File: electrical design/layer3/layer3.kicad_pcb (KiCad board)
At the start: 2 copper layers, 150 x 137.9 mm, 33 parts, among them J1 SH1.0 5P, J10 SH1.0 2P, J11 LAYER1, J2 SH1.0 5P, J3 SH1.0 5P, J4 SH1.0 5P, J5 XH2.54 5P, J6 CAMERA1, J7 CAMERA2, J8 COMPASS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

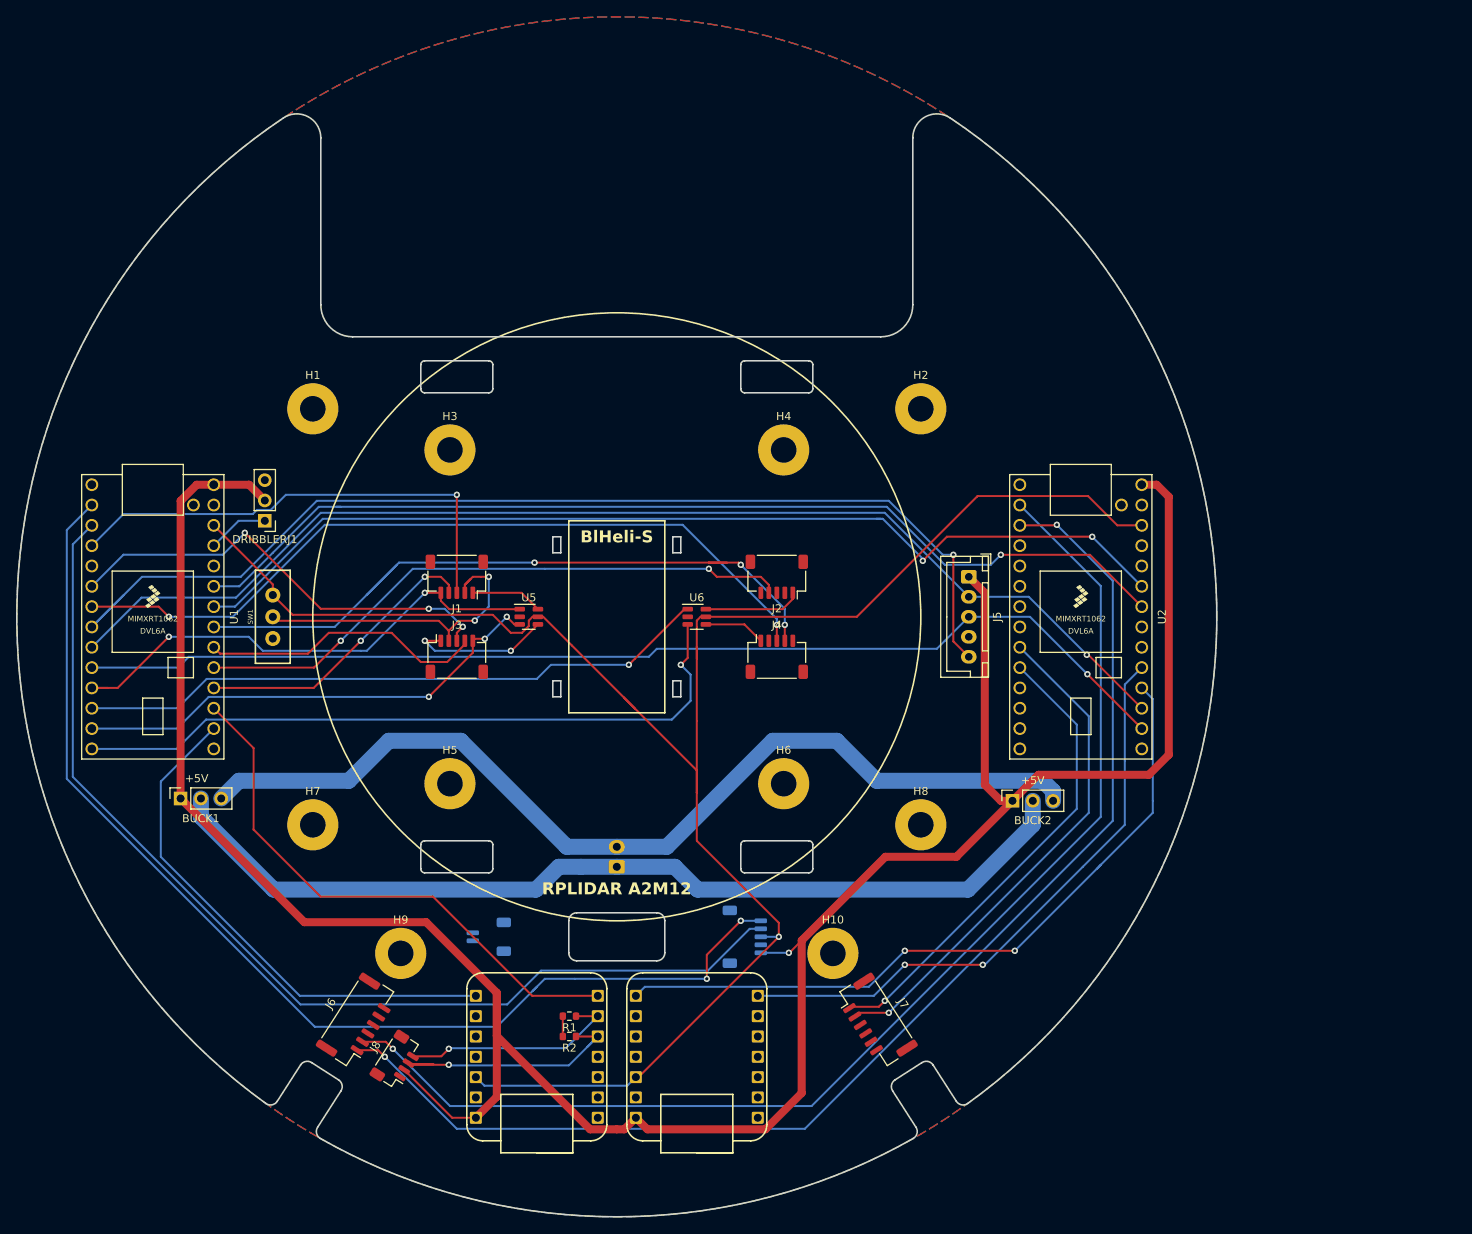
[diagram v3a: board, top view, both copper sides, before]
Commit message: update pcbs for dual camera design
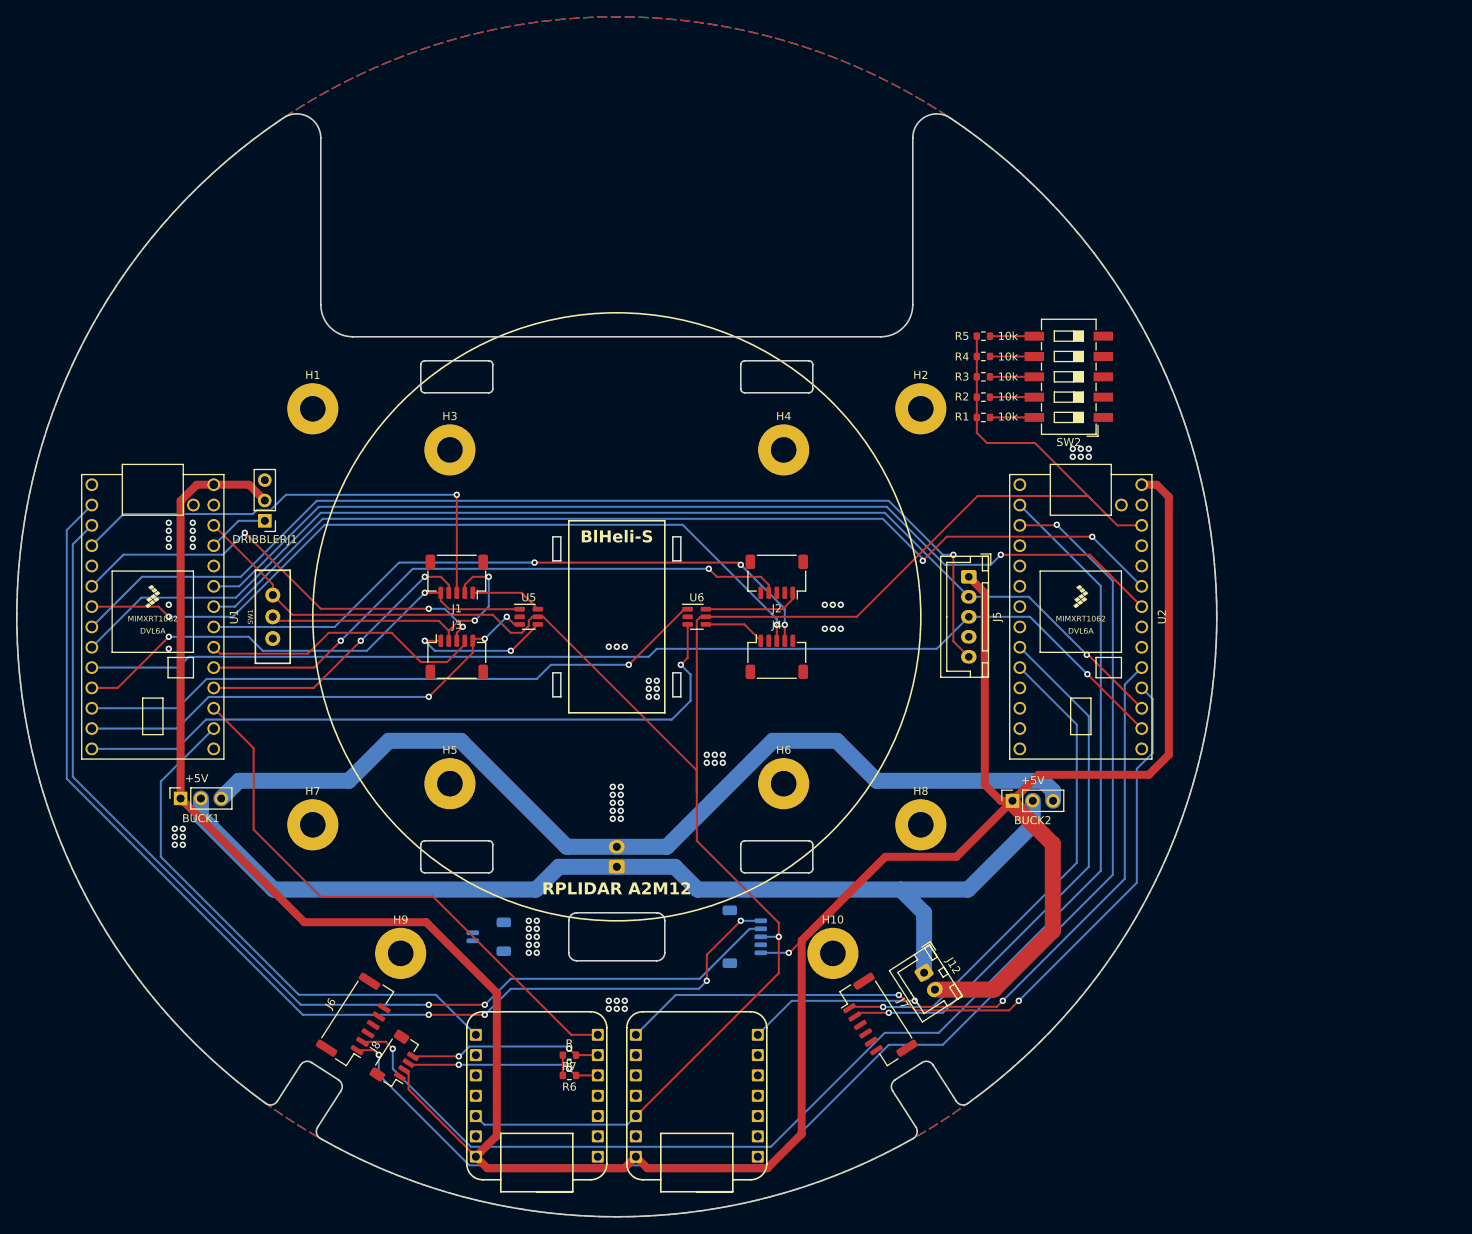
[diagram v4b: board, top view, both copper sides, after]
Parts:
- added J12: XH2.54 2P, Connector_JST:JST_XH_B2B-XH-A_1x02_P2.50mm_Vertical, F.Cu at (143.4, 149.5)
- added R1: 10k, Resistor_SMD:R_0603_1608Metric, F.Cu at (150.8, 80.1)
- added R2: 10k, Resistor_SMD:R_0603_1608Metric, F.Cu at (150.8, 77.5)
- added R3: 10k, Resistor_SMD:R_0603_1608Metric, F.Cu at (150.8, 75.0)
- added R4: 10k, Resistor_SMD:R_0603_1608Metric, F.Cu at (150.8, 72.5)
- added R5: 10k, Resistor_SMD:R_0603_1608Metric, F.Cu at (150.8, 69.9)
- added SW2: SW_DIP_x05, Button_Switch_SMD:SW_DIP_SPSTx05_Slide_6.7x14.26mm_W8.61mm_P2.54mm_LowProfile, F.Cu at (161.5, 75.0)
- J9: value Conn_01x02_Pin -> XH2.54 2P
- moved R6 4.87 mm to (99.1, 162.3)
- moved R7 4.87 mm to (99.1, 159.8)
- moved U3 4.87 mm to (95.0, 164.9)
- moved U4 4.87 mm to (115.0, 164.9)
- renumbered R2 to R6, R1 to R7
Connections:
- U2 pad 2: unconnected-(U2-Pad2) -> /STRAT1
- U2 pad 3: unconnected-(U2-Pad3) -> /STRAT2
- U2 pad 4: unconnected-(U2-Pad4) -> /STRAT3
- U2 pad 5: unconnected-(U2-Pad5) -> /STRAT4
- U2 pad 6: unconnected-(U2-Pad6) -> /STRAT5
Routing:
- net +5V: track 326.2 -> 368.3 mm
- net +3V3: track 237.8 -> 268.8 mm
- net GNDPWR: track 118.8 -> 130.4 mm
- net /CAM1TX: track 153.9 -> 163.4 mm
- net /CAM1RX: track 159.0 -> 168.2 mm
- net /IMUSDA: track 33.0 -> 24.5 mm, vias 1 -> 2
- net /M4CS: track 88.7 -> 81.1 mm
- net /BTTX: track 91.0 -> 98.0 mm
- net /BTRX: track 75.3 -> 81.9 mm
- net /LIDARPWM: track 136.2 -> 130.6 mm
- net /STRAT5: track 0.00 -> 5.54 mm
- net /STRAT4: track 0.00 -> 5.54 mm
- net /STRAT3: track 0.00 -> 5.54 mm
- net /STRAT2: track 0.00 -> 5.54 mm
- net /STRAT1: track 0.00 -> 5.54 mm
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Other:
- outline, holes or cut-outs redrawn

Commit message: change EN switch to larger one
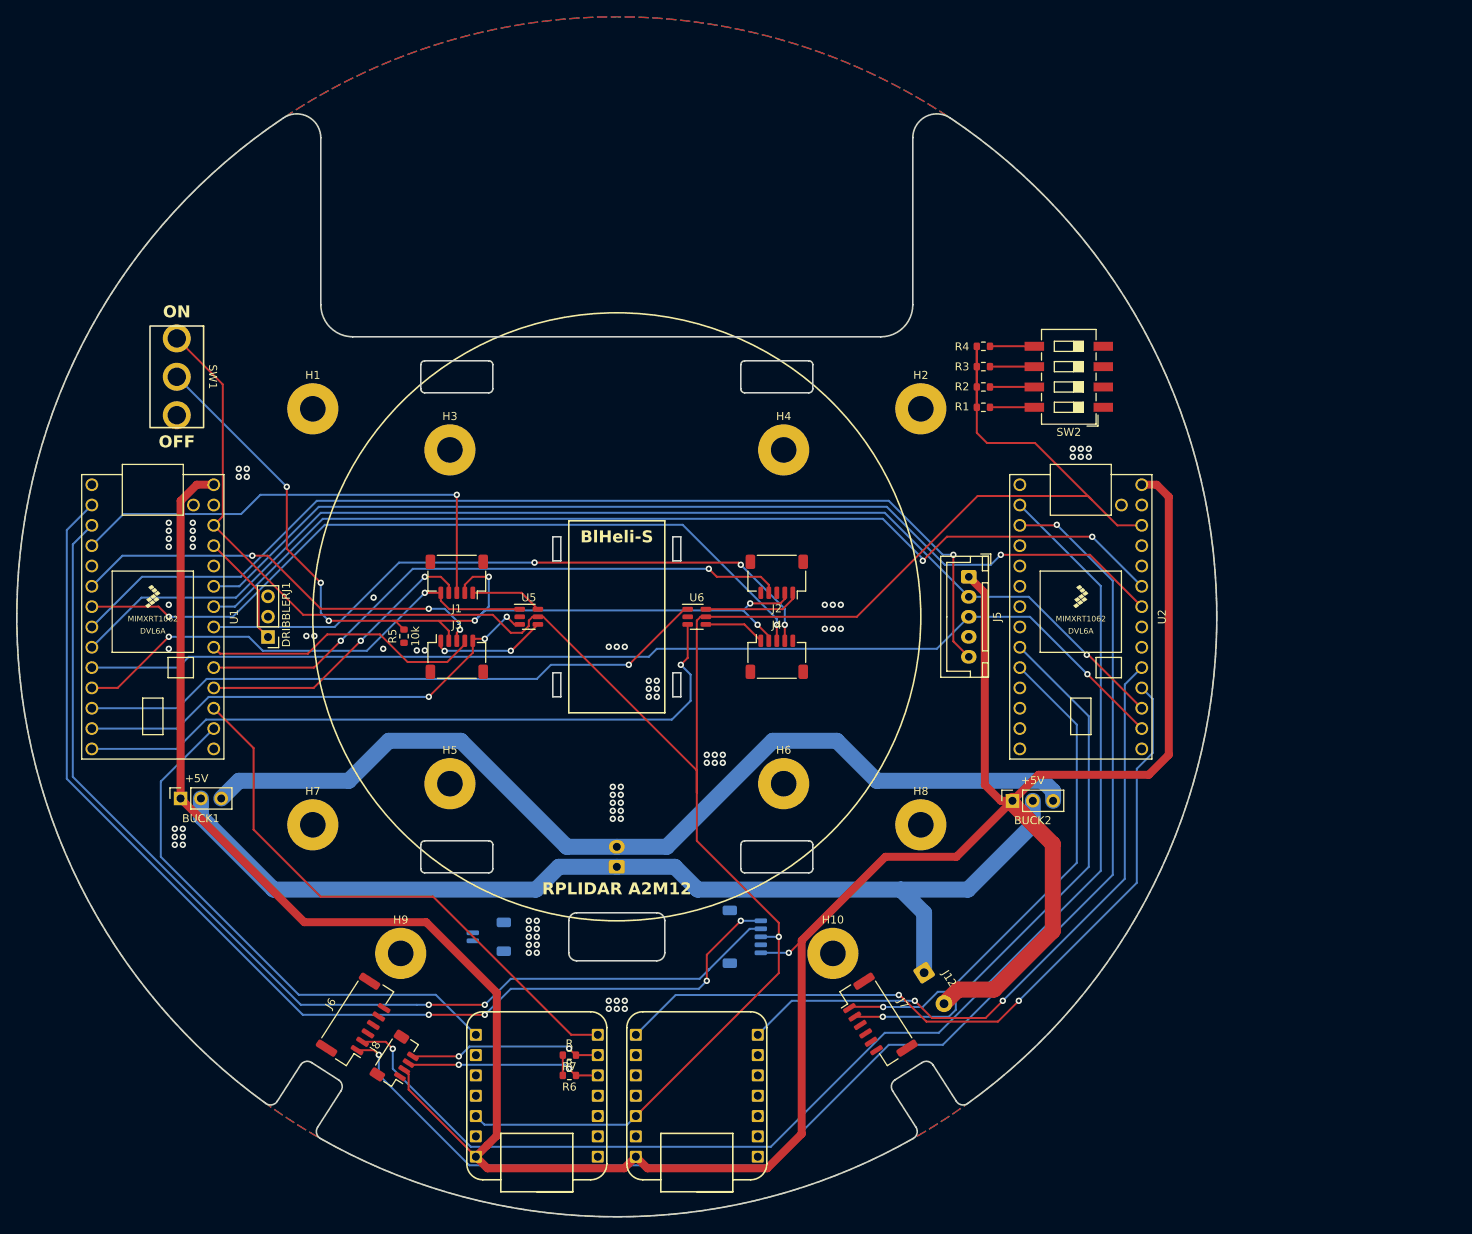
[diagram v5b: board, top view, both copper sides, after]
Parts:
- J12: footprint Connector_JST:JST_XH_B2B-XH-A_1x02_P2.50mm_Vertical -> Connector_Wire:SolderWire-0.5sqmm_1x02_P4.6mm_D0.9mm_OD2.1mm
- SW1: value SW_DPDT_x2 -> SW_SPDT; footprint Switches:SWITCH_SPDT_PTH_11.6X4.0MM_LOCK -> Switches:SWITCH_SPDT_PTH_12.7X6.7MM
- SW2: value SW_DIP_x05 -> SW_DIP_x04; footprint Button_Switch_SMD:SW_DIP_SPSTx05_Slide_6.7x14.26mm_W8.61mm_P2.54mm_LowProfile -> Button_Switch_SMD:SW_DIP_SPSTx04_Slide_6.7x11.72mm_W8.61mm_P2.54mm_LowProfile
- moved R5 81.6 mm to (78.4, 107.4), turned to 90 degrees
- moved SW1 32.3 mm to (50.0, 75.0), turned to -90 degrees
- moved DRIBBLERJ1 14.5 mm to (61.4, 107.5)
- moved R2 1.27 mm to (150.8, 76.3)
- moved R1 1.27 mm to (150.8, 78.8)
- moved R3 1.27 mm to (150.8, 73.7)
- moved R4 1.27 mm to (150.8, 71.2)
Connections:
- DRIBBLERJ1 pad 2: +5V -> unconnected-(DRIBBLERJ1-Pin_2-Pad2)
- R5 pad 1: +3V3 -> GNDD
- R5 pad 2: /STRAT5 -> /EN
- SW2 pad 5: GNDD -> /STRAT4
- SW2 pad 6: /STRAT5 -> /STRAT3
- SW2 pad 7: /STRAT4 -> /STRAT2
- SW2 pad 8: /STRAT3 -> /STRAT1
- U2 pad 6: /STRAT5 -> unconnected-(U2-Pad6)
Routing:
- net /EN: track 38.4 -> 117.9 mm, vias 2 -> 7
- net +3V3: track 268.8 -> 300.6 mm
- net +5V: track 368.3 -> 360.7 mm
- net /DRIBBLERPWM: track 7.67 -> 14.2 mm
- net /STRAT5: track 5.54 -> 0.00 mm
- net /M3INB: track 18.0 -> 14.5 mm
- net /M3PWM: track 56.1 -> 53.4 mm
- net /BTTX: track 98.0 -> 99.1 mm
- net /BTRX: track 81.9 -> 83.0 mm
- net /CAM2TX: track 68.0 -> 68.8 mm
- net GNDD: vias 69 -> 79
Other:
- board text added: "OFF"
- board text added: "ON"

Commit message: route layer 3
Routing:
- net /STRAT4: track 5.54 -> 48.2 mm, vias 0 -> 1
- net /STRAT3: track 5.55 -> 40.1 mm, vias 0 -> 1
- net /STRAT2: track 5.55 -> 31.0 mm, vias 0 -> 1
- net /STRAT1: track 5.55 -> 25.9 mm, vias 0 -> 1
- net /CAM1RX: track 168.2 -> 174.0 mm
- net /CAM1TX: track 163.4 -> 168.5 mm, vias 1 -> 2
- net /RX: track 126.7 -> 128.5 mm
- net /M1PWM: track 60.5 -> 59.0 mm
- net +3V3: track 300.6 -> 300.0 mm

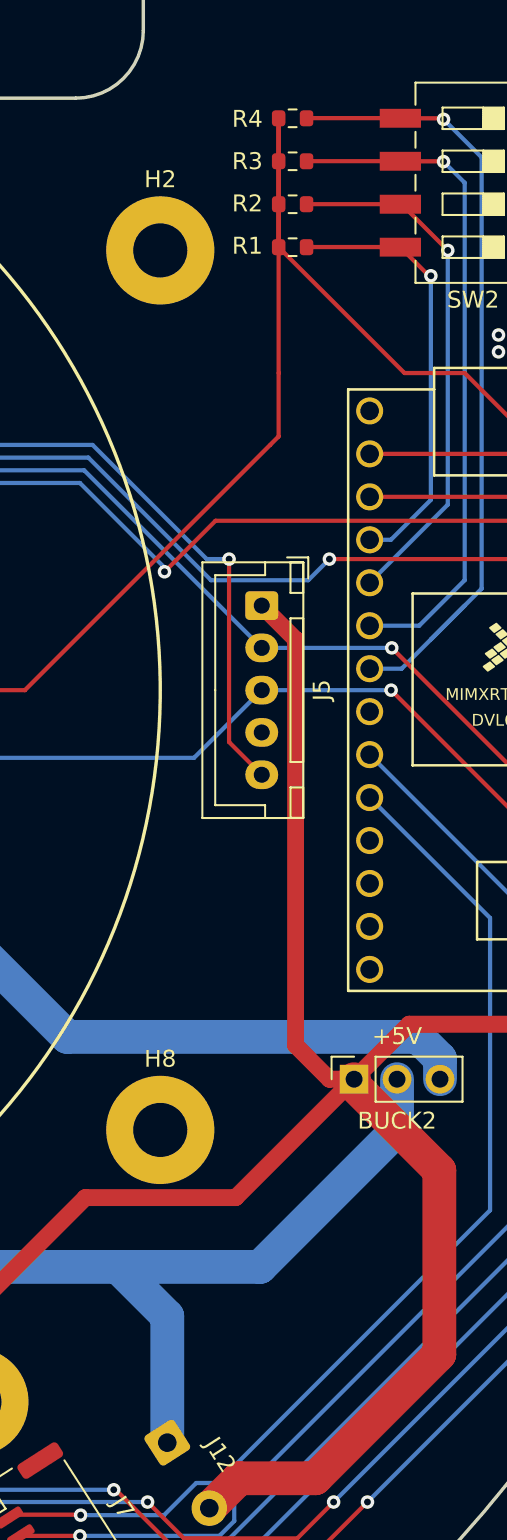
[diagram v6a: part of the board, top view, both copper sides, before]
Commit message: add 5v test point on l3
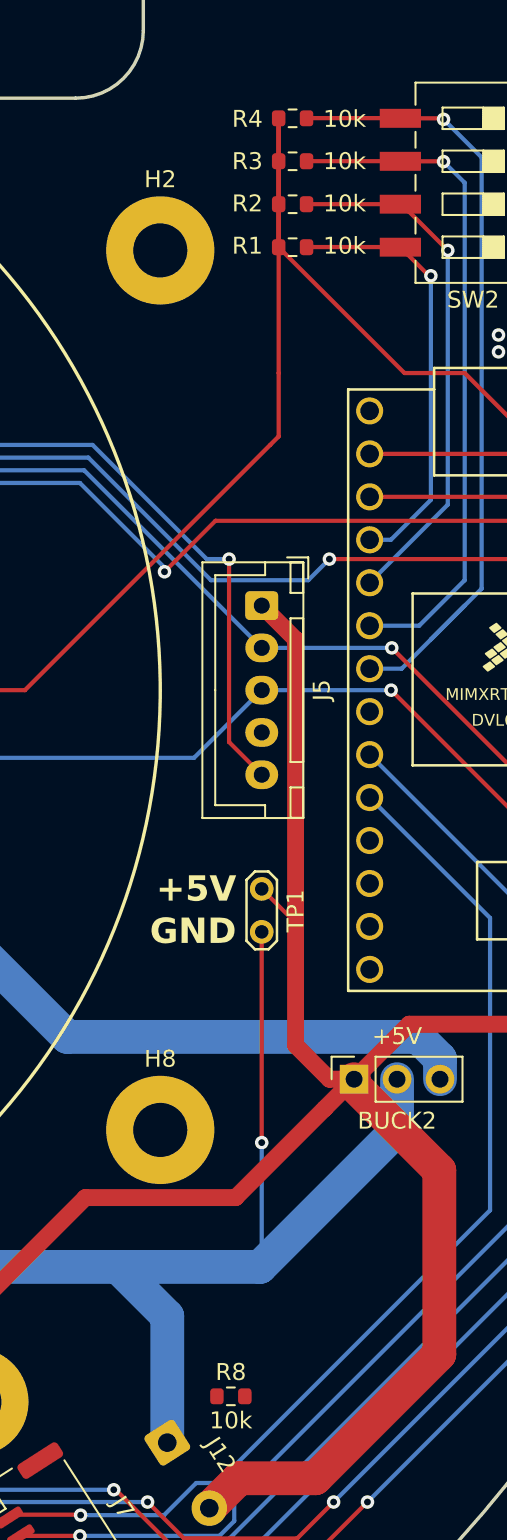
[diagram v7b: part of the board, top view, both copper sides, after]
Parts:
- added R8: 10k, Resistor_SMD:R_0603_1608Metric, F.Cu at (147.2, 146.8)
- added TP1: TestPoint_2Pole, TestPoint:TestPoint_2Pads_Pitch2.54mm_Drill0.8mm, F.Cu at (149.0, 116.8)
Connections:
- J12 pad 2: +5V -> Net-(J12-Pin_2)
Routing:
- net GNDPWR: track 130.4 -> 150.2 mm, vias 0 -> 1
- net +5V: track 360.7 -> 370.3 mm
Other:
- board text added: "+5V"
- board text added: "GND"
